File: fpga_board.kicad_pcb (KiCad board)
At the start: 8 copper layers, 50 x 50 mm, 6 parts, among them U1 LFE5U-85F-8BG381I, U2 CYUSB3014-BZXC, U3 K4B4G1646E-BCMA, U4 K4B4G1646E-BCMA, U5 K4B4G1646E-BCMA, U6 K4B4G1646E-BCMA

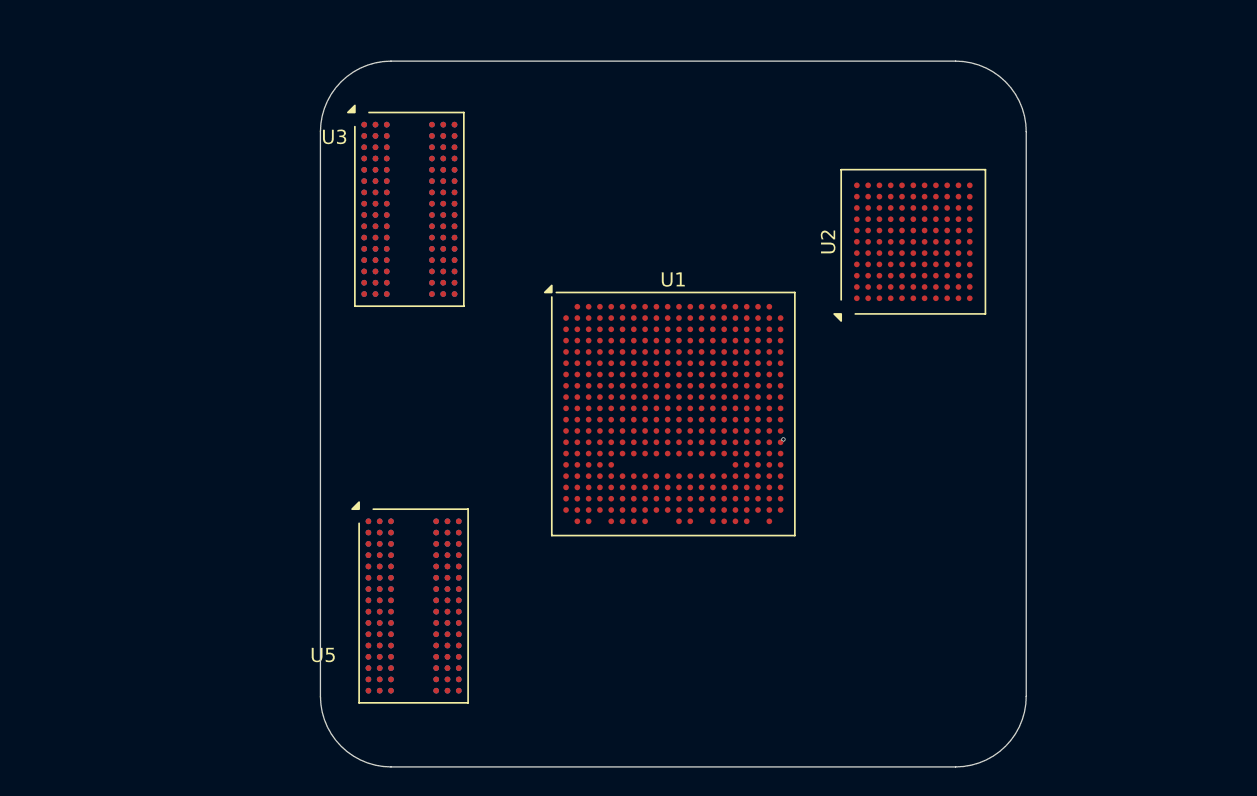
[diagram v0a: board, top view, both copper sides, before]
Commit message: changed FPGA to 45k cuz old one went out of stock :(
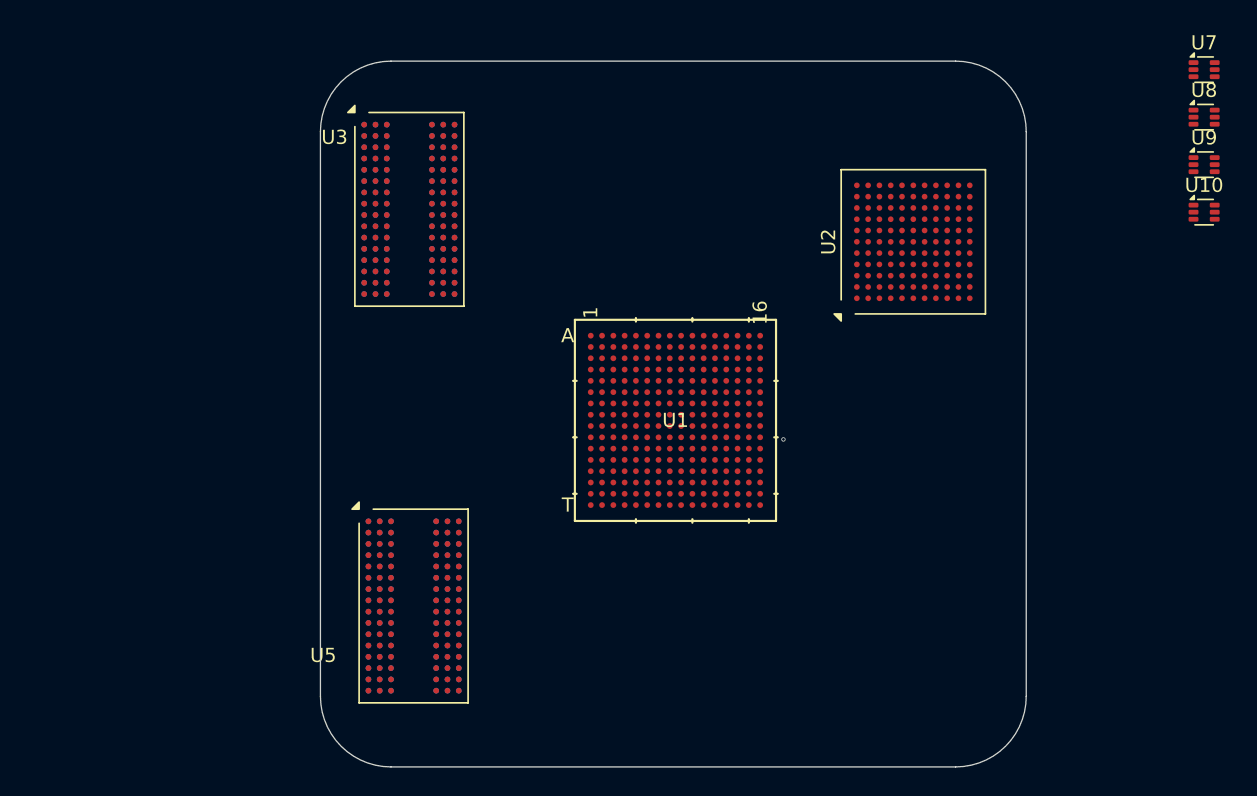
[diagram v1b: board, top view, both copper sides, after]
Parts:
- added U10: TLV62569DRL, Package_TO_SOT_SMD:SOT-563, F.Cu at (132.6, 50.7)
- added U7: TLV62569DRL, Package_TO_SOT_SMD:SOT-563, F.Cu at (132.6, 40.6)
- added U8: TLV62569DRL, Package_TO_SOT_SMD:SOT-563, F.Cu at (132.6, 44.0)
- added U9: TLV62569DRL, Package_TO_SOT_SMD:SOT-563, F.Cu at (132.6, 47.3)
- U1: value LFE5U-85F-8BG381I -> LFE5U-45F-7BG256I; footprint Package_BGA:Lattice_caBGA-381_17.0x17.0mm_Layout20x20_P0.8mm_Ball0.4mm_Pad0.4mm_NSMD -> ECP5:caBGA256_LAT
- moved U1 0.47 mm to (95.2, 65.5)
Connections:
- U1 pad A16: unconnected-(U1C-PT110A-PadA16) -> GND
- U1 pad D15: unconnected-(U1C-PT107A-PadD15) -> GND
- U1 pad D2: unconnected-(U1A-PL38C-PadD2) -> GND
- U1 pad F10: unconnected-(U1E-VCCIO0-PadF10) -> Net-(U1D-VCCIO1-PadF10)
- U1 pad F11: unconnected-(U1E-VCCIO1-PadF11) -> Net-(U1D-VCCIO1-PadF10)
- U1 pad F6: unconnected-(U1E-VCCAUX-PadF6) -> Net-(U1D-VCCIO0-PadF6)
- U1 pad F7: unconnected-(U1E-GND-PadF7) -> Net-(U1D-VCCIO0-PadF6)
- U1 pad F8: unconnected-(U1E-GND-PadF8) -> GND
- U1 pad F9: unconnected-(U1E-VCCIO0-PadF9) -> GND
- U1 pad G10: unconnected-(U1F-GND-PadG10) -> GND
- U1 pad G11: unconnected-(U1F-GND-PadG11) -> Net-(U1D-VCCAUX-PadG11)
- U1 pad G6: unconnected-(U1E-GND-PadG6) -> 1v1
- U1 pad G7: unconnected-(U1E-GND-PadG7) -> 1v1
- U1 pad G8: unconnected-(U1E-GND-PadG8) -> GND
- U1 pad G9: unconnected-(U1F-GND-PadG9) -> 1v1
- U1 pad H1: unconnected-(U1A-PL53C-PadH1) -> GND
- U1 pad H10: unconnected-(U1E-VCC-PadH10) -> GND
- U1 pad H11: unconnected-(U1E-VCC-PadH11) -> Net-(U1D-VCCIO2-PadH11)
- U1 pad H16: unconnected-(U1B-PR17D-PadH16) -> GND
- U1 pad H6: unconnected-(U1E-VCCIO7-PadH6) -> Net-(U1D-VCCIO7-PadH6)
- U1 pad H7: unconnected-(U1E-VCCIO7-PadH7) -> Net-(U1D-VCCIO7-PadH6)
- U1 pad H8: unconnected-(U1E-VCC-PadH8) -> GND
- U1 pad H9: unconnected-(U1E-VCC-PadH9) -> GND
- U1 pad J10: unconnected-(U1F-GND-PadJ10) -> GND
- U1 pad J11: unconnected-(U1F-GND-PadJ11) -> Net-(U1D-VCCIO2-PadH11)
- U1 pad J6: unconnected-(U1E-VCCIO7-PadJ6) -> Net-(U1D-VCCIO6-PadJ6)
- U1 pad J7: unconnected-(U1F-GND-PadJ7) -> Net-(U1D-VCCIO6-PadJ6)
- U1 pad J8: unconnected-(U1E-VCC-PadJ8) -> GND
- U1 pad J9: unconnected-(U1F-GND-PadJ9) -> GND
- U1 pad K10: unconnected-(U1F-GND-PadK10) -> GND
- U1 pad K11: unconnected-(U1G-GND-PadK11) -> Net-(U1D-VCCIO3-PadK11)
- U1 pad K6: unconnected-(U1F-GND-PadK6) -> GND
- U1 pad K7: unconnected-(U1F-GND-PadK7) -> GND
- U1 pad K8: unconnected-(U1E-VCC-PadK8) -> GND
- U1 pad K9: unconnected-(U1F-GND-PadK9) -> GND
- U1 pad L10: unconnected-(U1G-GND-PadL10) -> 1v1
- U1 pad L11: unconnected-(U1G-GND-PadL11) -> Net-(U1D-VCCIO3-PadK11)
- U1 pad L7: unconnected-(U1E-VCCIO6-PadL7) -> Net-(U1D-VCCAUX-PadG11)
- U1 pad L8: unconnected-(U1E-VCC-PadL8) -> 1v1
- U1 pad L9: unconnected-(U1F-GND-PadL9) -> 1v1
- U1 pad N10: unconnected-(U1E-VCC-PadN10) -> Net-(U1A-CFG_0)
- U1 pad N15: unconnected-(U1G-GND-PadN15) -> GND
- U1 pad N2: unconnected-(U1B-PL89A-PadN2) -> GND
- U1 pad P10: unconnected-(U1E-VCCIO8-PadP10) -> Net-(U1A-CFG_1)
- U1 pad T1: unconnected-(U1A-PB4B-PadT1) -> GND
- U1 pad T12: unconnected-(U1G-GND-PadT12) -> GND
- U1 pad T16: unconnected-(U1B-PR77A-PadT16) -> GND
- U1 pad T5: unconnected-(U1A-TCK-PadT5) -> GND
- U2 pad A1: unconnected-(U2C-U3VSSQ-PadA1) -> GND
- U2 pad A2: unconnected-(U2C-U3RXVDDQ-PadA2) -> Net-(U2C-U3RXVDDQ)
- U2 pad A3: unconnected-(U2A-SSRXM-PadA3) -> SS_RX_M
- U2 pad A4: unconnected-(U2A-SSRXP-PadA4) -> SS_RX_P
- U2 pad A5: unconnected-(U2A-SSTXP-PadA5) -> Net-(U2A-SSTXP)
- U2 pad A6: unconnected-(U2A-SSTXM-PadA6) -> Net-(U2A-SSTXM)
- U2 pad A7: unconnected-(U2C-AVDD-PadA7) -> Net-(U2C-AVDD)
- U2 pad A8: unconnected-(U2C-VSS-PadA8) -> GND
- U2 pad B10: unconnected-(U2C-VDD-PadB10) -> FX3_1v2
- U2 pad B2: unconnected-(U2A-FSLC[0]-PadB2) -> Net-(U2A-FSLC[0])
- U2 pad B3: unconnected-(U2B-R_USB3-PadB3) -> Net-(U2B-R_USB3)
- U2 pad B4: unconnected-(U2A-FSLC[1]-PadB4) -> Net-(U2A-FSLC[1])
- U2 pad B5: unconnected-(U2C-U3TXVDDQ-PadB5) -> Net-(U2C-U3TXVDDQ)
- U2 pad B6: unconnected-(U2C-CVDDQ-PadB6) -> Net-(U2C-CVDDQ)
- U2 pad B7: unconnected-(U2C-AVSS-PadB7) -> GND
- U2 pad B8: unconnected-(U2C-VSS-PadB8) -> GND
- U2 pad B9: unconnected-(U2C-VSS-PadB9) -> GND
- U2 pad C1: unconnected-(U2B-GPIO[54]-PadC1) -> SPI_SSN
- U2 pad C11: unconnected-(U2B-VIO5-PadC11) -> Net-(U2B-VIO5)
- U2 pad C2: unconnected-(U2B-GPIO[55]-PadC2) -> SPI_MISO
- U2 pad C3: unconnected-(U2C-VDD-PadC3) -> FX3_1v2
- U2 pad C6: unconnected-(U2B-XTALIN-PadC6) -> FX3_XTALIN
- U2 pad C7: unconnected-(U2A-XTALOUT-PadC7) -> FX3_XTALOUT
- U2 pad C8: unconnected-(U2B-R_USB2-PadC8) -> Net-(U2B-R_USB2)
- U2 pad D4: unconnected-(U2B-GPIO[53]-PadD4) -> SPI_SCK
- U2 pad D5: unconnected-(U2B-GPIO[56]-PadD5) -> SPI_MOSI
- U2 pad D8: unconnected-(U2C-VSS-PadD8) -> GND
- U2 pad E1: unconnected-(U2B-GPIO[47]-PadE1) -> FIFO_DQ29
- U2 pad E10: unconnected-(U2C-VBATT-PadE10) -> 5v_VBUS
- U2 pad E11: unconnected-(U2C-VBUS-PadE11) -> 5v_VBUS
- U2 pad E2: unconnected-(U2C-VSS-PadE2) -> GND
- U2 pad E4: unconnected-(U2B-GPIO[49]-PadE4) -> FIFO_DQ31
- U2 pad E5: unconnected-(U2B-GPIO[48]-PadE5) -> FIFO_DQ30
- U2 pad E6: unconnected-(U2A-FSLC[2]-PadE6) -> Net-(U2A-FSLC[2])
- U2 pad E9: unconnected-(U2C-VDD-PadE9) -> FX3_1v2
- U2 pad F1: unconnected-(U2B-VIO2-PadF1) -> FX3_VIO1-2_3v3
- U2 pad F10: unconnected-(U2B-GPIO[0]-PadF10) -> FIFO_DQ0
- U2 pad F11: unconnected-(U2C-VDD-PadF11) -> FX3_1v2
- U2 pad F3: unconnected-(U2B-GPIO[44]-PadF3) -> FIFO_DQ27
- U2 pad F4: unconnected-(U2B-GPIO[41]/A0_[5]-PadF4) -> FIFO_DQ24
- U2 pad F5: unconnected-(U2B-GPIO[46]-PadF5) -> FIFO_DQ28
- U2 pad F7: unconnected-(U2B-GPIO[2]-PadF7) -> FIFO_DQ2
- U2 pad F8: unconnected-(U2B-GPIO[5]-PadF8) -> FIFO_DQ5
- U2 pad F9: unconnected-(U2B-GPIO[1]-PadF9) -> FIFO_DQ1
- U2 pad G1: unconnected-(U2C-VSS-PadG1) -> GND
- U2 pad G10: unconnected-(U2B-GPIO[3]-PadG10) -> FIFO_DQ3
- U2 pad G11: unconnected-(U2C-VSS-PadG11) -> GND
- U2 pad G2: unconnected-(U2B-GPIO[42]/A1_[5]-PadG2) -> FIFO_DQ25
- U2 pad G3: unconnected-(U2B-GPIO[43]-PadG3) -> FIFO_DQ26
- U2 pad G4: unconnected-(U2B-GPIO[30]-PadG4) -> Net-(U2B-GPIO[30])
- U2 pad G6: unconnected-(U2B-GPIO[22]-PadG6) -> FIFO_FLAGB
- U2 pad G7: unconnected-(U2B-GPIO[21]-PadG7) -> FIFO_FLAGA
- U2 pad G8: unconnected-(U2B-GPIO[15]-PadG8) -> FIFO_DQ15
- U2 pad G9: unconnected-(U2B-GPIO[4]-PadG9) -> FIFO_DQ4
- U2 pad H1: unconnected-(U2C-VDD-PadH1) -> FX3_1v2
- U2 pad H10: unconnected-(U2B-GPIO[6]-PadH10) -> FIFO_DQ6
- U2 pad H11: unconnected-(U2B-VIO1-PadH11) -> FX3_VIO1-2_3v3
- U2 pad H2: unconnected-(U2B-GPIO[39]-PadH2) -> FIFO_DQ22
- U2 pad H3: unconnected-(U2B-GPIO[40]-PadH3) -> FIFO_DQ23
- U2 pad H4: unconnected-(U2B-GPIO[31]-PadH4) -> Net-(U2B-GPIO[31])
- U2 pad H5: unconnected-(U2B-GPIO[29]-PadH5) -> FIFO_A0
- U2 pad H7: unconnected-(U2B-GPIO[20]-PadH7) -> FIFO_SLRD#
- U2 pad H8: unconnected-(U2B-GPIO[24]-PadH8) -> FIFO_PKTEND#
- U2 pad H9: unconnected-(U2B-GPIO[7]-PadH9) -> FIFO_DQ7
- U2 pad J1: unconnected-(U2B-GPIO[38]-PadJ1) -> FIFO_DQ21
- U2 pad J10: unconnected-(U2B-GPIO[8]-PadJ10) -> FIFO_DQ8
- U2 pad J11: unconnected-(U2C-VDD-PadJ11) -> FX3_1v2
- U2 pad J2: unconnected-(U2B-GPIO[36]-PadJ2) -> FIFO_DQ19
- U2 pad J3: unconnected-(U2B-GPIO[37]-PadJ3) -> FIFO_DQ20
- U2 pad J4: unconnected-(U2B-GPIO[34]-PadJ4) -> FIFO_DQ17
- U2 pad J5: unconnected-(U2B-GPIO[28]-PadJ5) -> FIFO_A1
- U2 pad J6: unconnected-(U2B-GPIO[16]-PadJ6) -> FIFO_CLK
- U2 pad J7: unconnected-(U2B-GPIO[19]-PadJ7) -> FIFO_SLOE#
- U2 pad J8: unconnected-(U2B-GPIO[14]-PadJ8) -> FIFO_DQ14
- U2 pad J9: unconnected-(U2B-GPIO[9]-PadJ9) -> FIFO_DQ9
- U2 pad K1: unconnected-(U2B-GPIO[35]-PadK1) -> FIFO_DQ18
- U2 pad K10: unconnected-(U2B-GPIO[12]-PadK10) -> FIFO_DQ12
- U2 pad K11: unconnected-(U2B-GPIO[10]-PadK11) -> FIFO_DQ10
- U2 pad K2: unconnected-(U2B-GPIO[33]-PadK2) -> FIFO_DQ16
- U2 pad K3: unconnected-(U2C-VSS-PadK3) -> GND
- U2 pad K4: unconnected-(U2C-VSS-PadK4) -> GND
- U2 pad K7: unconnected-(U2B-GPIO[18]-PadK7) -> FIFO_SLWR#
- U2 pad K8: unconnected-(U2B-GPIO[17]-PadK8) -> FIFO_SLCS#
- U2 pad K9: unconnected-(U2B-GPIO[13]-PadK9) -> FIFO_DQ13
- U2 pad L1: unconnected-(U2C-VSS-PadL1) -> GND
- U2 pad L10: unconnected-(U2B-GPIO[11]-PadL10) -> FIFO_DQ11
- U2 pad L11: unconnected-(U2C-VSS-PadL11) -> GND
- U2 pad L2: unconnected-(U2C-VSS-PadL2) -> GND
- U2 pad L3: unconnected-(U2C-VSS-PadL3) -> GND
- U2 pad L5: unconnected-(U2C-VDD-PadL5) -> FX3_1v2
- U2 pad L6: unconnected-(U2C-VSS-PadL6) -> GND
- U2 pad L7: unconnected-(U2C-VDD-PadL7) -> FX3_1v2
- U2 pad L9: unconnected-(U2B-VIO1-PadL9) -> FX3_VIO1-2_3v3
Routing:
- net unconnected-(U1B-PR83B-PadN20): vias 1 -> 0
- net (no net): vias 0 -> 1

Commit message: added colors and bunch of other stuff idk
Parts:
- U6: moved to F.Cu
- moved U4 27.9 mm to (52.7, 65.3)
- moved U3 18.8 mm to (57.5, 50.6)
- moved U6 15.9 mm to (79.5, 63.0), turned to -90 degrees
- moved U5 6.46 mm to (79.5, 72.8), turned to -90 degrees
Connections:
- U1 pad B1: unconnected-(U1A-PL11A-PadB1) -> BYTE_LANE_0_0
- U1 pad B2: unconnected-(U1A-PL11B-PadB2) -> BYTE_LANE_0_1
- U1 pad C1: unconnected-(U1A-PL14A-PadC1) -> BYTE_LANE_0_2
- U1 pad C2: unconnected-(U1A-PL14B-PadC2) -> BYTE_LANE_0_3
- U1 pad C3: unconnected-(U1A-PL11C-PadC3) -> BYTE_LANE_0_4
- U1 pad D1: unconnected-(U1A-PL17A-PadD1) -> DQS0_P
- U1 pad D3: unconnected-(U1A-PL11D-PadD3) -> BYTE_LANE_0_5
- U1 pad E2: unconnected-(U1A-PL17B-PadE2) -> DQS0_N
- U1 pad E3: unconnected-(U1A-PL14C-PadE3) -> BYTE_LANE_0_6
- U1 pad F3: unconnected-(U1A-PL14D-PadF3) -> BYTE_LANE_0_7
- U1 pad H11: Net-(U1D-VCCIO2-PadH11) -> 1v35
- U1 pad H6: Net-(U1D-VCCIO7-PadH6) -> 1v35
- U1 pad H7: Net-(U1D-VCCIO7-PadH6) -> 1v35
- U1 pad J11: Net-(U1D-VCCIO2-PadH11) -> 1v35
- U1 pad J6: Net-(U1D-VCCIO6-PadJ6) -> 1v35
- U1 pad J7: Net-(U1D-VCCIO6-PadJ6) -> 1v35
- U1 pad K11: Net-(U1D-VCCIO3-PadK11) -> 1v35
- U1 pad L11: Net-(U1D-VCCIO3-PadK11) -> 1v35
- U5 pad A2: unconnected-(U5A-DQU5-PadA2) -> BYTE_LANE_3_5
- U5 pad A3: unconnected-(U5A-DQU7-PadA3) -> BYTE_LANE_3_7
- U5 pad A7: unconnected-(U5A-DQU4-PadA7) -> BYTE_LANE_3_4
- U5 pad B7: unconnected-(U5A-*DQSU-PadB7) -> DQS3_N
- U5 pad B8: unconnected-(U5A-DQU6-PadB8) -> BYTE_LANE_3_6
- U5 pad C2: unconnected-(U5A-DQU3-PadC2) -> BYTE_LANE_3_3
- U5 pad C3: unconnected-(U5A-DQU1-PadC3) -> BYTE_LANE_3_1
- U5 pad C7: unconnected-(U5A-DQSU-PadC7) -> DQS3_P
- U5 pad C8: unconnected-(U5A-DQU2-PadC8) -> BYTE_LANE_3_2
- U5 pad D7: unconnected-(U5A-DQU0-PadD7) -> BYTE_LANE_3_0
- U5 pad E3: unconnected-(U5A-DQL0-PadE3) -> BYTE_LANE_2_0
- U5 pad F2: unconnected-(U5A-DQL2-PadF2) -> BYTE_LANE_2_2
- U5 pad F3: unconnected-(U5A-DQSL-PadF3) -> DQS2_P
- U5 pad F7: unconnected-(U5A-DQL1-PadF7) -> BYTE_LANE_2_1
- U5 pad F8: unconnected-(U5A-DQL3-PadF8) -> BYTE_LANE_2_3
- U5 pad G2: unconnected-(U5A-DQL6-PadG2) -> BYTE_LANE_2_6
- U5 pad G3: unconnected-(U5A-*DQSL-PadG3) -> DQS2_N
- U5 pad H3: unconnected-(U5A-DQL4-PadH3) -> BYTE_LANE_2_4
- U5 pad H7: unconnected-(U5A-DQL7-PadH7) -> BYTE_LANE_2_7
- U5 pad H8: unconnected-(U5A-DQL5-PadH8) -> BYTE_LANE_2_5
- U6 pad A1: unconnected-(U6B-VDDQ-PadA1) -> 1v35
- U6 pad A2: unconnected-(U6A-DQU5-PadA2) -> BYTE_LANE_1_5
- U6 pad A3: unconnected-(U6A-DQU7-PadA3) -> BYTE_LANE_1_7
- U6 pad A7: unconnected-(U6A-DQU4-PadA7) -> BYTE_LANE_1_4
- U6 pad A8: unconnected-(U6B-VDDQ-PadA8) -> 1v35
- U6 pad A9: unconnected-(U6C-VSS-PadA9) -> GND
- U6 pad B1: unconnected-(U6C-VSSQ-PadB1) -> GND
- U6 pad B2: unconnected-(U6B-VDD-PadB2) -> 1v35
- U6 pad B3: unconnected-(U6C-VSS-PadB3) -> GND
- U6 pad B7: unconnected-(U6A-*DQSU-PadB7) -> DQS1_N
- U6 pad B8: unconnected-(U6A-DQU6-PadB8) -> BYTE_LANE_1_6
- U6 pad B9: unconnected-(U6C-VSSQ-PadB9) -> GND
- U6 pad C1: unconnected-(U6B-VDDQ-PadC1) -> 1v35
- U6 pad C2: unconnected-(U6A-DQU3-PadC2) -> BYTE_LANE_1_3
- U6 pad C3: unconnected-(U6A-DQU1-PadC3) -> BYTE_LANE_1_1
- U6 pad C7: unconnected-(U6A-DQSU-PadC7) -> DQS1_P
- U6 pad C8: unconnected-(U6A-DQU2-PadC8) -> BYTE_LANE_1_2
- U6 pad C9: unconnected-(U6B-VDDQ-PadC9) -> 1v35
- U6 pad D1: unconnected-(U6C-VSSQ-PadD1) -> GND
- U6 pad D2: unconnected-(U6B-VDDQ-PadD2) -> 1v35
- U6 pad D3: unconnected-(U6A-DMU-PadD3) -> DM1
- U6 pad D7: unconnected-(U6A-DQU0-PadD7) -> BYTE_LANE_1_0
- U6 pad D8: unconnected-(U6C-VSSQ-PadD8) -> GND
- U6 pad D9: unconnected-(U6B-VDD-PadD9) -> 1v35
- U6 pad E1: unconnected-(U6C-VSS-PadE1) -> GND
- U6 pad E2: unconnected-(U6C-VSSQ-PadE2) -> GND
- U6 pad E3: unconnected-(U6A-DQL0-PadE3) -> BYTE_LANE_0_0
- U6 pad E7: unconnected-(U6A-DML-PadE7) -> DM0
- U6 pad E8: unconnected-(U6C-VSSQ-PadE8) -> GND
- U6 pad E9: unconnected-(U6B-VDDQ-PadE9) -> 1v35
- U6 pad F1: unconnected-(U6B-VDDQ-PadF1) -> 1v35
- U6 pad F2: unconnected-(U6A-DQL2-PadF2) -> BYTE_LANE_0_2
- U6 pad F3: unconnected-(U6A-DQSL-PadF3) -> DQS0_P
- U6 pad F7: unconnected-(U6A-DQL1-PadF7) -> BYTE_LANE_0_1
- U6 pad F8: unconnected-(U6A-DQL3-PadF8) -> BYTE_LANE_0_3
- U6 pad F9: unconnected-(U6C-VSSQ-PadF9) -> GND
- U6 pad G1: unconnected-(U6C-VSSQ-PadG1) -> GND
- U6 pad G2: unconnected-(U6A-DQL6-PadG2) -> BYTE_LANE_0_6
- U6 pad G3: unconnected-(U6A-*DQSL-PadG3) -> DQS0_N
- U6 pad G7: unconnected-(U6B-VDD-PadG7) -> 1v35
- U6 pad G8: unconnected-(U6C-VSS-PadG8) -> GND
- U6 pad G9: unconnected-(U6C-VSSQ-PadG9) -> GND
- U6 pad H1: unconnected-(U6B-VREFDQ-PadH1) -> DRAM_VREF
- U6 pad H2: unconnected-(U6B-VDDQ-PadH2) -> 1v35
- U6 pad H3: unconnected-(U6A-DQL4-PadH3) -> BYTE_LANE_0_4
- U6 pad H7: unconnected-(U6A-DQL7-PadH7) -> BYTE_LANE_0_7
- U6 pad H8: unconnected-(U6A-DQL5-PadH8) -> BYTE_LANE_0_5
- U6 pad H9: unconnected-(U6B-VDDQ-PadH9) -> 1v35
- U6 pad J2: unconnected-(U6C-VSS-PadJ2) -> GND
- U6 pad J3: unconnected-(U6A-*RAS-PadJ3) -> #RAS
- U6 pad J7: unconnected-(U6A-CK-PadJ7) -> CK
- U6 pad J8: unconnected-(U6C-VSS-PadJ8) -> GND
- U6 pad K1: unconnected-(U6A-ODT-PadK1) -> ODT
- U6 pad K2: unconnected-(U6B-VDD-PadK2) -> 1v35
- U6 pad K3: unconnected-(U6A-*CAS-PadK3) -> #CAS
- U6 pad K7: unconnected-(U6A-*CK-PadK7) -> #CK
- U6 pad K8: unconnected-(U6B-VDD-PadK8) -> 1v35
- U6 pad K9: unconnected-(U6A-CKE-PadK9) -> CKE
- U6 pad L2: unconnected-(U6A-*CS-PadL2) -> #CS
- U6 pad L3: unconnected-(U6A-*WE-PadL3) -> #WE
- U6 pad L7: unconnected-(U6A-A10/AP-PadL7) -> A10
- U6 pad L8: unconnected-(U6B-ZQ-PadL8) -> Net-(U6B-ZQ)
- U6 pad M1: unconnected-(U6C-VSS-PadM1) -> GND
- U6 pad M2: unconnected-(U6A-BA0-PadM2) -> BA0
- U6 pad M3: unconnected-(U6A-BA2-PadM3) -> BA2
- U6 pad M8: unconnected-(U6B-VREFCA-PadM8) -> DRAM_VREF
- U6 pad M9: unconnected-(U6C-VSS-PadM9) -> GND
- U6 pad N1: unconnected-(U6B-VDD-PadN1) -> 1v35
- U6 pad N2: unconnected-(U6A-A3-PadN2) -> A3
- U6 pad N3: unconnected-(U6A-A0-PadN3) -> A0
- U6 pad N7: unconnected-(U6A-A12/*BC-PadN7) -> A12
- U6 pad N8: unconnected-(U6A-BA1-PadN8) -> BA1
- U6 pad N9: unconnected-(U6B-VDD-PadN9) -> 1v35
- U6 pad P1: unconnected-(U6C-VSS-PadP1) -> GND
- U6 pad P2: unconnected-(U6A-A5-PadP2) -> A5
- U6 pad P3: unconnected-(U6A-A2-PadP3) -> A2
- U6 pad P7: unconnected-(U6A-A1-PadP7) -> A1
- U6 pad P8: unconnected-(U6A-A4-PadP8) -> A4
- U6 pad P9: unconnected-(U6C-VSS-PadP9) -> GND
- U6 pad R1: unconnected-(U6B-VDD-PadR1) -> 1v35
- U6 pad R2: unconnected-(U6A-A7-PadR2) -> A7
- U6 pad R3: unconnected-(U6A-A9-PadR3) -> A9
- U6 pad R7: unconnected-(U6A-A11-PadR7) -> A11
- U6 pad R8: unconnected-(U6A-A6-PadR8) -> A6
- U6 pad R9: unconnected-(U6B-VDD-PadR9) -> 1v35
- U6 pad T1: unconnected-(U6C-VSS-PadT1) -> GND
- U6 pad T2: unconnected-(U6A-*RESET-PadT2) -> #RESET
- U6 pad T3: unconnected-(U6A-A13-PadT3) -> A13
- U6 pad T7: unconnected-(U6A-A14-PadT7) -> A14
- U6 pad T8: unconnected-(U6A-A8-PadT8) -> A8
- U6 pad T9: unconnected-(U6C-VSS-PadT9) -> GND
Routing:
- net DQS0_N: track 0.00 -> 9.79 mm
- net DQS0_P: track 0.00 -> 9.75 mm

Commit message: ddr wiring and other stuff
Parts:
- U4: moved to F.Cu
- moved U3 73.1 mm to (129.6, 63.1)
- moved U4 65.3 mm to (116.5, 79.0), turned to 0 degrees
- moved U2 18.6 mm to (94.5, 46.6), turned to 0 degrees
- moved U5 1.07 mm to (78.5, 72.3), turned to 90 degrees
- moved U6 1.04 mm to (78.5, 62.6), turned to 90 degrees
- moved U1 0.47 mm to (95.0, 65.0)
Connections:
- net FIFO_A0 renamed FIFO.A0
- net FIFO_A1 renamed FIFO.A1
- net FIFO_CLK renamed FIFO.CLK
- net FIFO_FLAGA renamed FIFO.FLAGA
- net FIFO_FLAGB renamed FIFO.FLAG_B
- net FIFO_PKTEND# renamed FIFO.PKTEND#
- net FIFO_SLCS# renamed FIFO.SLCS#
- net FIFO_SLOE# renamed FIFO.SLOE#
- net FIFO_SLRD# renamed FIFO.SLRD#
- net FIFO_SLWR# renamed FIFO.SLWR#
- net FX3_1v2 renamed 1v2
- U1 pad B1: BYTE_LANE_0_0 -> BYTE_LANE_0_5
- U1 pad C1: BYTE_LANE_0_2 -> DM0
- U1 pad C2: BYTE_LANE_0_3 -> BYTE_LANE_0_7
- U1 pad C3: BYTE_LANE_0_4 -> BYTE_LANE_0_3
- U1 pad D3: BYTE_LANE_0_5 -> BYTE_LANE_0_4
- U1 pad E3: BYTE_LANE_0_6 -> BYTE_LANE_0_0
- U1 pad F1: unconnected-(U1A-PL23A-PadF1) -> BYTE_LANE_1_6
- U1 pad F3: BYTE_LANE_0_7 -> BYTE_LANE_0_6
- U1 pad G1: unconnected-(U1A-PL29A-PadG1) -> DQS1_P
- U1 pad G4: unconnected-(U1A-PL20B-PadG4) -> BYTE_LANE_0_2
- U1 pad H2: unconnected-(U1A-PL29B-PadH2) -> DQS1_N
- U1 pad H4: unconnected-(U1A-PL26B-PadH4) -> BYTE_LANE_1_0
- U1 pad J1: unconnected-(U1A-PL32A-PadJ1) -> BYTE_LANE_1_4
- U1 pad J3: unconnected-(U1A-PL29C-PadJ3) -> BYTE_LANE_1_2
- U1 pad J4: unconnected-(U1A-PL26C-PadJ4) -> DM1
- U1 pad J5: unconnected-(U1A-PL26D-PadJ5) -> BYTE_LANE_1_3
- U1 pad K1: unconnected-(U1A-PL32C-PadK1) -> BYTE_LANE_1_1
- U1 pad K2: unconnected-(U1A-PL32D-PadK2) -> BYTE_LANE_1_7
- U1 pad K3: unconnected-(U1A-PL29D-PadK3) -> BYTE_LANE_1_5
- U5 pad D3: unconnected-(U5A-DMU-PadD3) -> DM3
- U5 pad E7: unconnected-(U5A-DML-PadE7) -> DM2
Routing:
- net BYTE_LANE_0_4: track 0.00 -> 20.4 mm
- net BYTE_LANE_1_5: track 0.00 -> 20.1 mm, vias 0 -> 2
- net BYTE_LANE_1_3: track 0.00 -> 19.5 mm, vias 0 -> 2
- net BYTE_LANE_1_0: track 0.00 -> 19.4 mm, vias 0 -> 2
- net BYTE_LANE_0_0: track 0.00 -> 19.2 mm
- net BYTE_LANE_1_2: track 0.00 -> 19.1 mm, vias 0 -> 2
- net BYTE_LANE_1_7: track 0.00 -> 19.1 mm, vias 0 -> 2
- net DM1: track 0.00 -> 18.4 mm, vias 0 -> 2
- net DQS1_N: track 0.00 -> 18.4 mm, vias 0 -> 2
- net BYTE_LANE_1_4: track 0.00 -> 18.3 mm, vias 0 -> 2
- net BYTE_LANE_1_6: track 0.00 -> 17.6 mm, vias 0 -> 2
- net BYTE_LANE_0_2: track 0.00 -> 17.5 mm
- net BYTE_LANE_0_1: track 0.00 -> 17.5 mm
- net BYTE_LANE_0_6: track 0.00 -> 17.5 mm
- net DQS1_P: track 0.00 -> 17.5 mm, vias 0 -> 2
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- added copper zone on In1.Cu, net GND
